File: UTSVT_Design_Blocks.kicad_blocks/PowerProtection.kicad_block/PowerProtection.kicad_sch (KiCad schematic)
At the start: 16 parts, among them IC1 LM74502DDFR, Q1 PSMN012-100YS, Q2 PSMN012-100YS

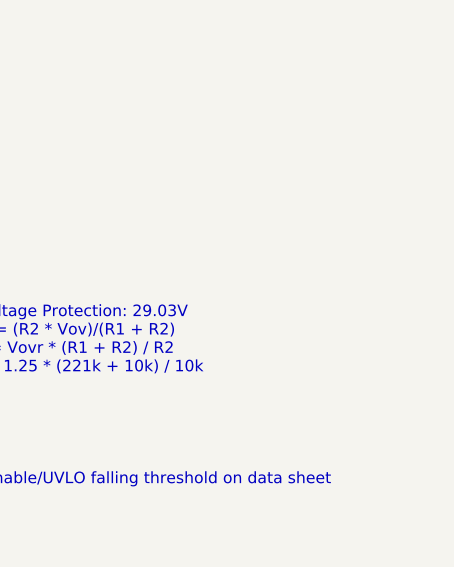
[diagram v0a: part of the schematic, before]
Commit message: fixed unvlo and made source and gate hieracrhical labels
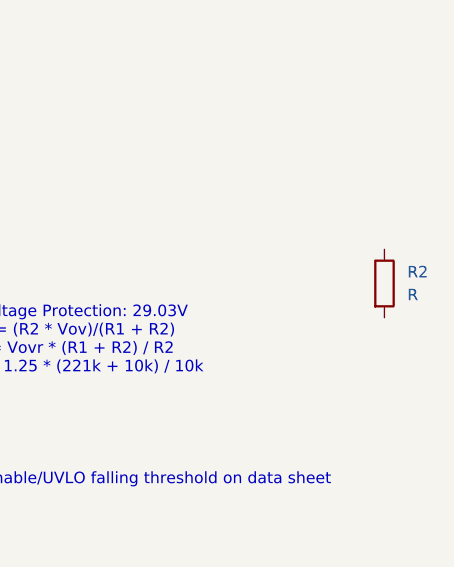
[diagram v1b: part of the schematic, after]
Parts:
- added R2: R, symbol Device:R
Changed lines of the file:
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@@
+		)
+	)
+	(symbol
+		(lib_id "Device:R")
+		(at 170.18 68.58 0)
+		(unit 1)
+		(exclude_from_sim no)
+		(in_bom yes)
+		(on_board yes)
+		(dnp no)
+		(fields_autoplaced yes)
+		(property "Reference" "R2"
+			(at 172.72 67.3099 0)
+			(effects
+				(font
+					(size 1.27 1.27)
+				)
+				(justify left)
+			)
+		)
+		(property "Value" "R"
+			(at 172.72 69.8499 0)
+			(effects
+				(font
+					(size 1.27 1.27)
+				)
+				(justify left)
+			)
+		)
+		(property "Footprint" ""
+			(at 168.402 68.58 90)
+			(effects
+				(font
+					(size 1.27 1.27)
+				)
+				(hide yes)
+			)
+		)
+		(property "Datasheet" "~"
+			(at 170.18 68.58 0)
+			(effects
+				(font
+					(size 1.27 1.27)
+				)
+				(hide yes)
+			)
+		)
+		(property "Description" "Resistor"
+			(at 170.18 68.58 0)
+			(effects
+				(font
+					(size 1.27 1.27)
+				)
+				(hide yes)
+			)
+		)
+		(pin "2"
+		)
+		(pin "1"
+		)
+		(instances
+			(project ""
+				(path "/a968d2b9-0c0e-491c-a5a4-aacd8448ff64"
+					(reference "R2")
+					(unit 1)
+				)
+			)
 		)
 	)

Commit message: fixed unvlo and made source and gate hieracrhical labels
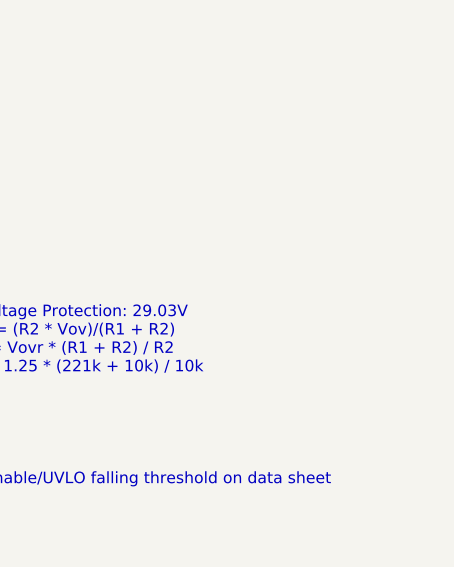
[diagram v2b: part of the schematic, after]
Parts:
- removed R2: R, symbol Device:R
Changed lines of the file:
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@@
-		)
-	)
-	(symbol
-		(lib_id "Device:R")
-		(at 170.18 68.58 0)
-		(unit 1)
-		(exclude_from_sim no)
-		(in_bom yes)
-		(on_board yes)
-		(dnp no)
-		(fields_autoplaced yes)
-		(property "Reference" "R2"
-			(at 172.72 67.3099 0)
-			(effects
-				(font
-					(size 1.27 1.27)
-				)
-				(justify left)
-			)
-		)
-		(property "Value" "R"
-			(at 172.72 69.8499 0)
-			(effects
-				(font
-					(size 1.27 1.27)
-				)
-				(justify left)
-			)
-		)
-		(property "Footprint" ""
-			(at 168.402 68.58 90)
-			(effects
-				(font
-					(size 1.27 1.27)
-				)
-				(hide yes)
-			)
-		)
-		(property "Datasheet" "~"
-			(at 170.18 68.58 0)
-			(effects
-				(font
-					(size 1.27 1.27)
-				)
-				(hide yes)
-			)
-		)
-		(property "Description" "Resistor"
-			(at 170.18 68.58 0)
-			(effects
-				(font
-					(size 1.27 1.27)
-				)
-				(hide yes)
-			)
-		)
-		(pin "2"
-		)
-		(pin "1"
-		)
-		(instances
-			(project ""
-				(path "/a968d2b9-0c0e-491c-a5a4-aacd8448ff64"
-					(reference "R2")
-					(unit 1)
-				)
-			)
 		)
 	)
